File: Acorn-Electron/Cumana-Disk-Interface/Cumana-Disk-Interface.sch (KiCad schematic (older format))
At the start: 54 parts, among them J1 Bottom Top, J2 CONN_12X2, J3 Conn_01x34_Female, Q2 Q_NPN_CBE, Q3 Q_NPN_CBE, Q4 Q_PNP_CBE, Q5 Q_NPN_CBE, U1 74LS138, U10 74LS174, U11 M5W1793-02P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

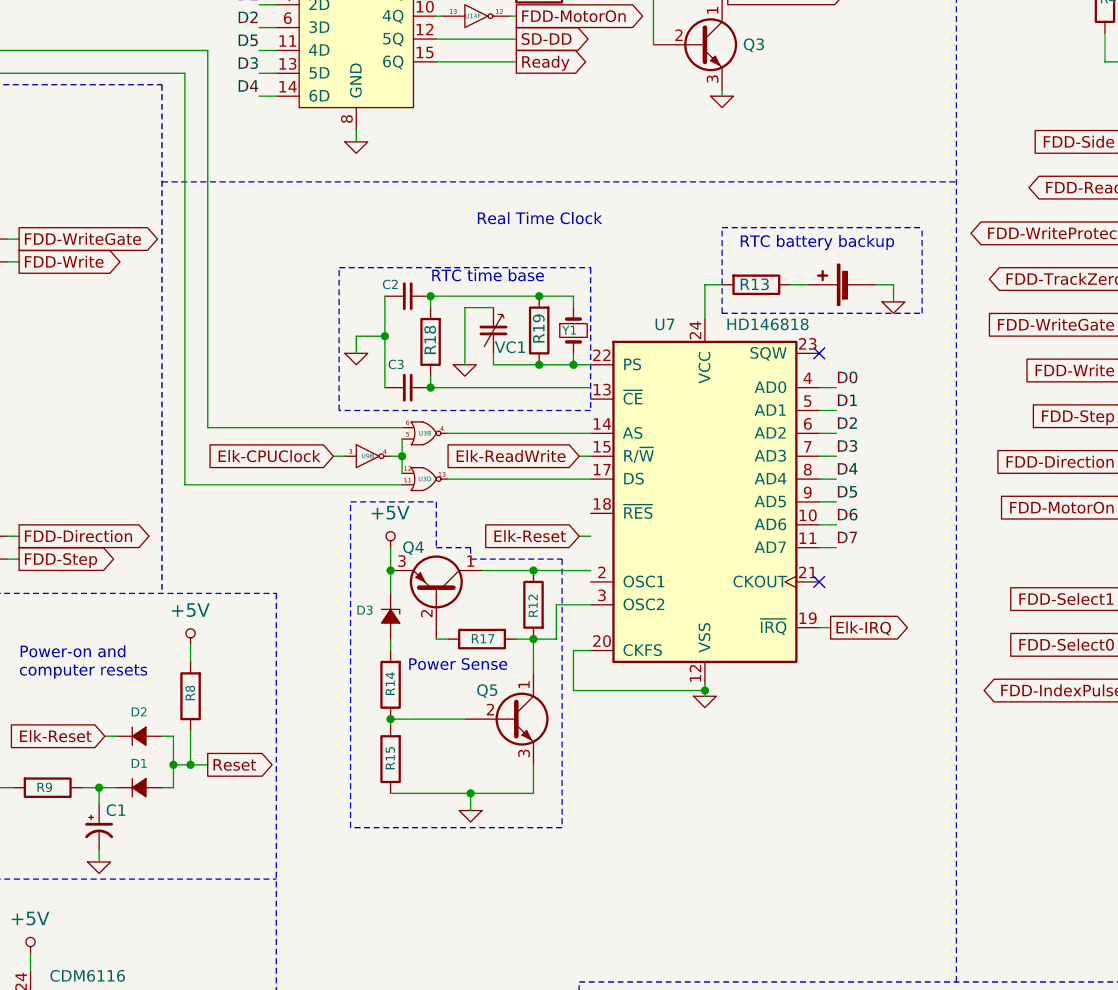
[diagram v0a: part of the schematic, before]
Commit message: Cumana disk interface - charge battery
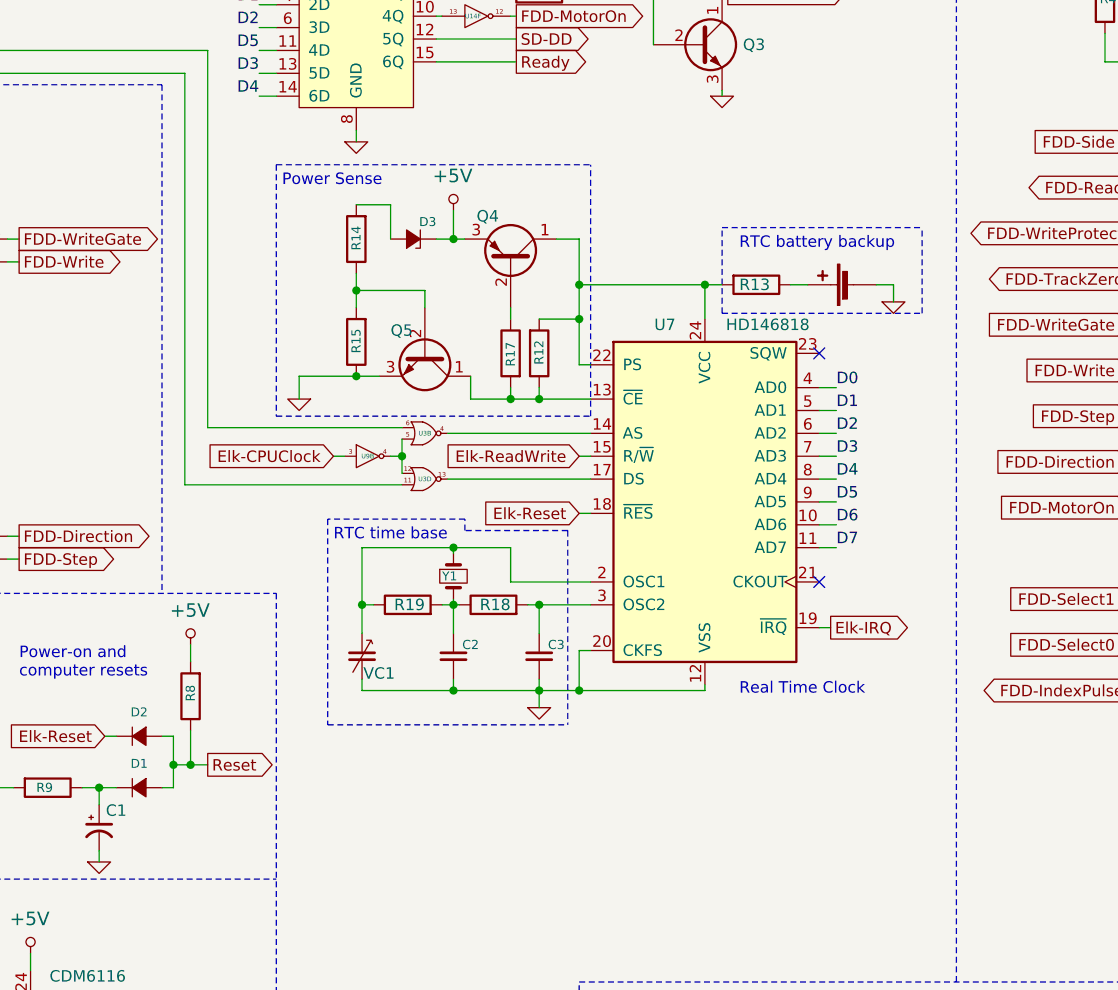
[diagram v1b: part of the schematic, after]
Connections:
- net Elk-Reset: now also U7.18 (~RES)
- net GND: now also C2.1, C3.1, VC1.2; no longer C2.2, C3.2, VC1.1
- net at U7.13 (~CE): now also Q5.1 (C), R12.1, R17.2
- net at U7.2 (OSC1): now also R19.1, VC1.1, Y1.1
- net at R13.2, U7.24 (VCC): now also Q4.1 (C), R12.2, U7.22 (PS)
- net at R18.1: now also C2.2, R19.2, Y1.2; no longer C3.1
- new net: C3.2, R18.2, U7.3 (OSC2)
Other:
- moved on the sheet: C2, C3, D3, Q4, Q5, R12, R14, R15, R17, R18, R19, VC1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

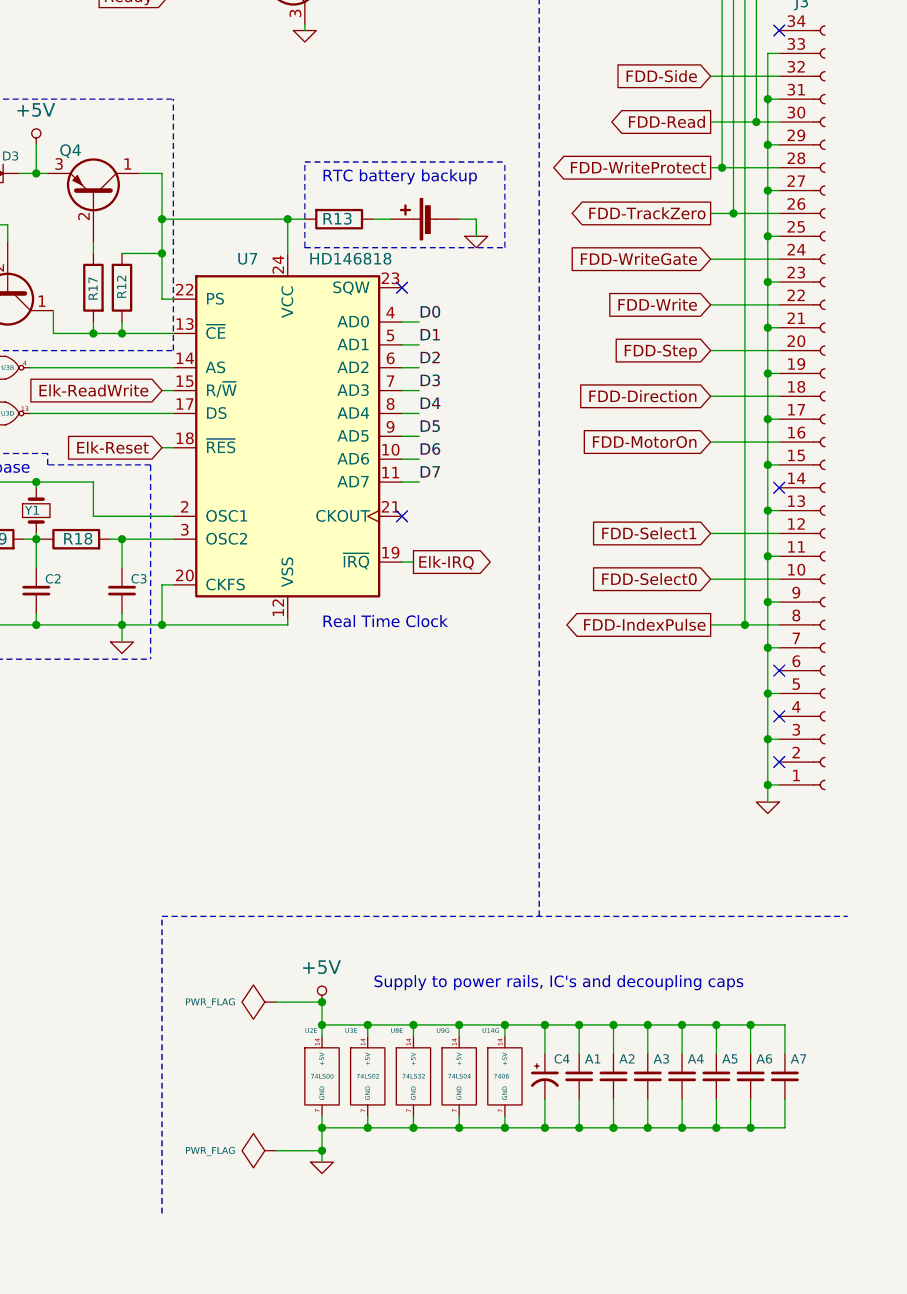
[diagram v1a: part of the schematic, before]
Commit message: corrections and footptint selections
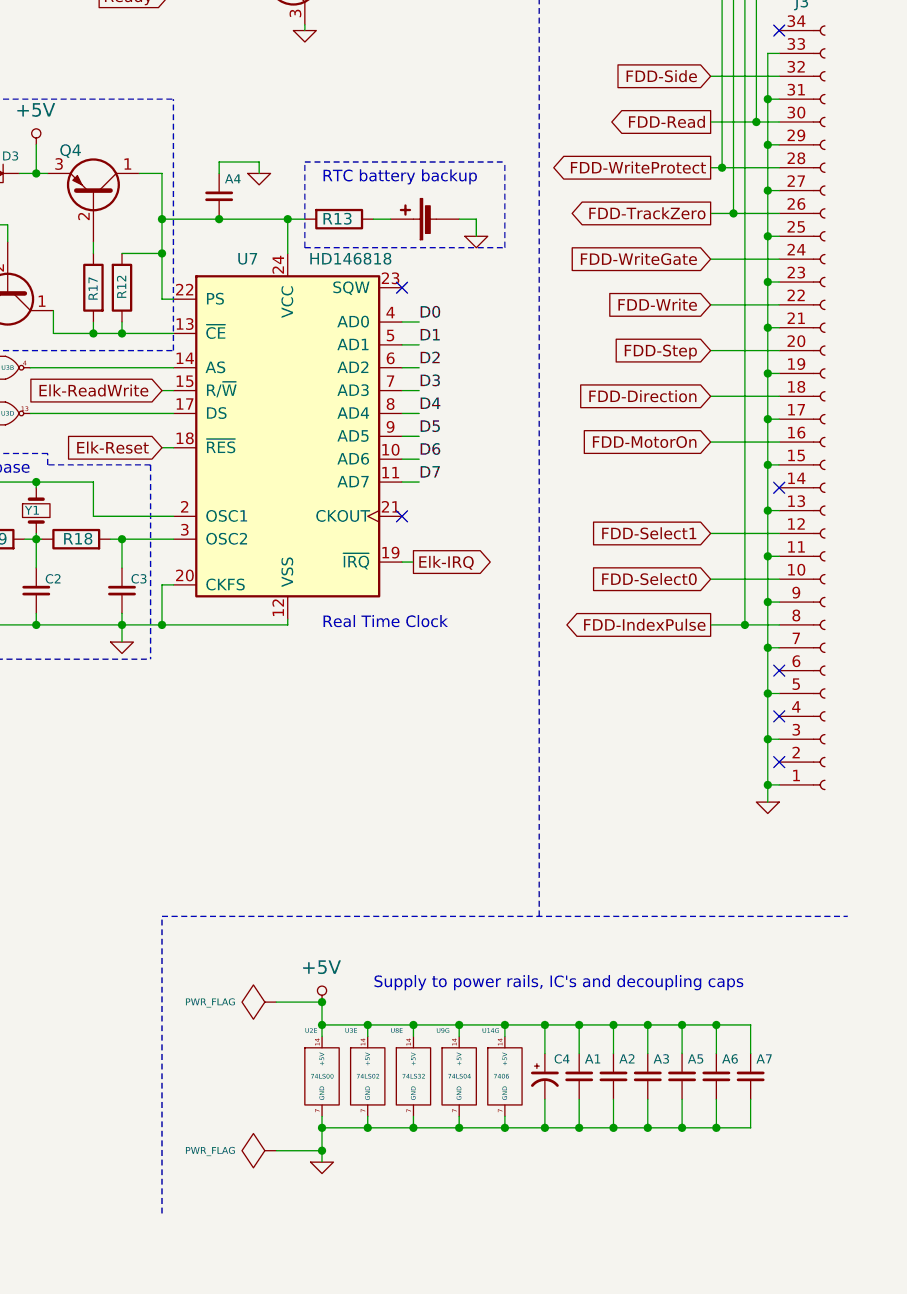
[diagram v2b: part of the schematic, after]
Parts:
- A1, A2, A3, A4, A5, A6, A7: footprint (none) -> Cumana-Disk-Interface:C_Disc_D8.0mm_W2.5mm_P5.00mm
- C1, C4: footprint (none) -> Cumana-Disk-Interface:CP_Radial_Tantal_D4.5mm_P5.00mm
- C2, C3: footprint (none) -> Cumana-Disk-Interface:C_Disc_D4.3mm_W1.9mm_P5.00mm
- D1, D2, D3: footprint (none) -> Cumana-Disk-Interface:D_DO-34_SOD68_P10.16mm_Horizontal
- J1: footprint (none) -> Cumana-Disk-Interface:Connector_2x9_P1.27mm_Polarized_Edge
- J2: footprint (none) -> Cumana-Disk-Interface:Connector_2x12_P1.27mm_Polarized_Edge
- J3: footprint (none) -> Cumana-Disk-Interface:IDC-Header_2x17_P2.54mm_Horizontal_Lock
- Q2, Q3, Q4, Q5: footprint (none) -> Cumana-Disk-Interface:TO-92
- R1, R12, R13, R14, R15, R17, R18, R19, R2, R20, R3, R4, R5, R6, R7, R8, R9: footprint (none) -> Cumana-Disk-Interface:R_Axial_DIN0212_L12.5mm_D2.5mm_Horizontal
- U1, U10, U12: footprint (none) -> Cumana-Disk-Interface:DIP-16_W7.62mm
- U11: footprint Package_DIP:DIP-40_W15.24mm -> Cumana-Disk-Interface:DIP-40_W15.24mm_Socket
- U13: footprint (none) -> Cumana-Disk-Interface:DIP-8_W7.62mm
- U14, U2, U3, U8, U9: footprint (none) -> Cumana-Disk-Interface:DIP-14_W7.62mm
- U4, U5: footprint Package_DIP:DIP-40_W15.24mm -> Cumana-Disk-Interface:DIP-28_W15.24mm_Socket
- U6, U7: footprint Package_DIP:DIP-40_W15.24mm -> Cumana-Disk-Interface:DIP-24_W15.24mm
- VC1: value C_Variable -> C_Trimmer; footprint (none) -> Cumana-Disk-Interface:C_Trimmer
- Y1: footprint (none) -> Cumana-Disk-Interface:Crystal_D3.0mm_Vertical
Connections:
- net +5V: no longer A4.1
- net GND: now also A4.1; no longer A4.2
- net at Q4.1 (C), R12.2, R13.2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: now also A4.2
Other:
- moved on the sheet: A4, A5, A6, A7

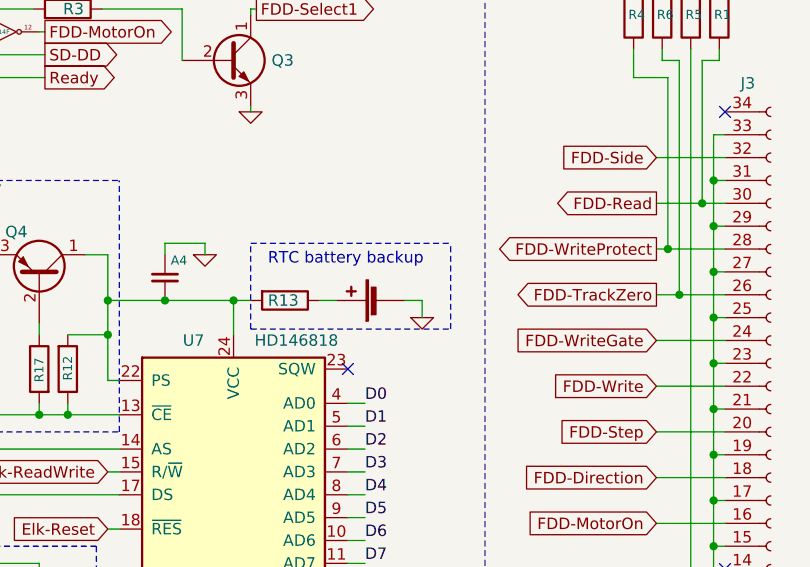
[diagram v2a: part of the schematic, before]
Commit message: added footprints and pcb
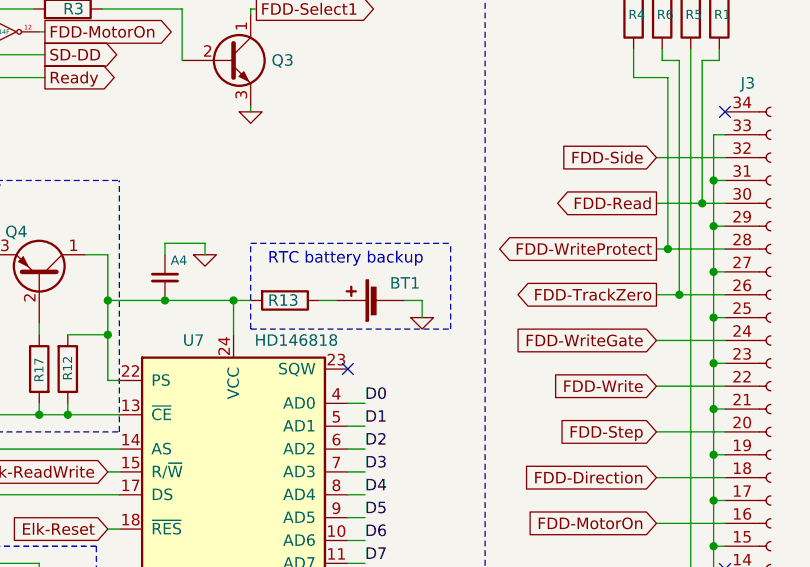
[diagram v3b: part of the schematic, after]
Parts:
- added BT1: Battery_Cell, Cumana-Disk-Interface:Battery_Cell, symbol Cumana-Disk-Interface:Battery_Cell
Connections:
- net GND: now also BT1.2 (-)
- net at R13.1: now also BT1.1 (+)
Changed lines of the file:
@@
 Sheet 1 1
 Title "Acorn Electron - Cumana Disk Interface"
-Date "2023-08-21"
+Date "2023-09-05"
 Rev ""
 Comp "www.benningtons.net"
@@
 Connection ~ 8925 6075
 Connection ~ 8925 6525
-$Comp
-L Cumana-Disk-Interface:Battery_Cell #BT01
-U 1 1 65EFF647
-P 9425 2550
-F 0 "#BT01" V 9588 2600 50  0001 C CNN
-F 1 "Battery_Cell" V 9589 2600 50  0001 C CNN
-F 2 "" V 9425 2610 50  0001 C CNN
-F 3 "~" V 9425 2610 50  0001 C CNN
-	1    9425 2550
-	0    -1   -1   0
-$EndComp
 Connection ~ 8925 5975
 Wire Wire Line
@@
 Wire Wire Line
 	8650 2300 8650 2350
+$Comp
+L Cumana-Disk-Interface:Battery_Cell BT1
+U 1 1 65017FC0
+P 9425 2550
+F 0 "BT1" V 9500 2450 50  0000 C CNN
+F 1 "Battery_Cell" V 9589 2600 50  0001 C CNN
+F 2 "Cumana-Disk-Interface:Battery_Cell" V 9425 2610 50  0001 C CNN
+F 3 "~" V 9425 2610 50  0001 C CNN
+	1    9425 2550
+	0    -1   -1   0
+$EndComp
 $EndSCHEMATC

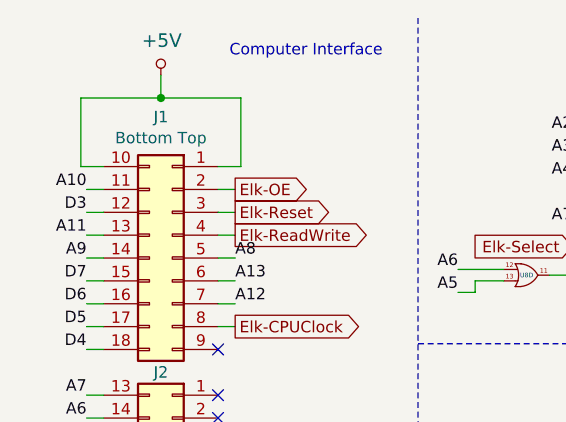
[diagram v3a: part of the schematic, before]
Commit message: bill of materials added
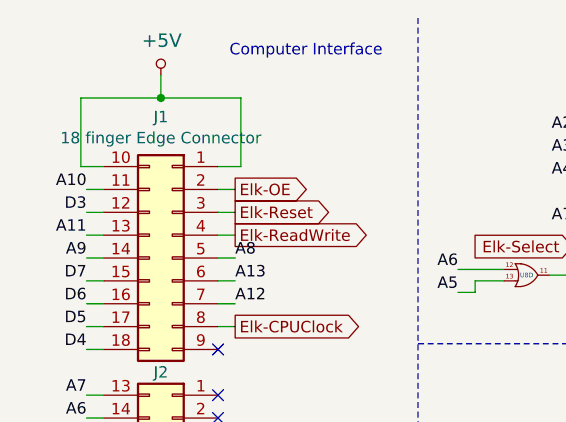
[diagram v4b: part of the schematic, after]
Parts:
- A1, A2, A3, A4, A5, A6, A7: value C -> 0.01uF
- BT1: value Battery_Cell -> 3.6v 100mAh
- C1: value CP1 -> 1uF 25V
- C2, C3: value C -> 33pF
- C4: value CP1 -> 10uF 6.3V
- D1, D2: value Diode -> Small Signal Diode
- D3: value D_Zener -> 3.9V Zener
- J1: value Bottom Top -> 18 finger Edge Connector
- J2: value CONN_12X2 -> 24 finger Edge Connector
- J3: value Conn_01x34_Female -> 34-way IDC header
- Q2, Q3, Q5: value Q_NPN_CBE -> BC337
- Q4: value Q_PNP_CBE -> BC327
- R1: value R -> 150
- R12: value R -> 100k
- R13: value R -> 1k
- R14: value R -> 120
- R15, R17: value R -> 470
- R18: value R -> 150k
- R19: value R -> 5.6M
- R2, R20, R3, R4, R5, R6: value R -> 2.2k
- R7, R8, R9: value R -> 10k
- VC1: value C_Trimmer -> 2 - 30pF
- Y1: value Crystal_Small -> 32.768kHz
